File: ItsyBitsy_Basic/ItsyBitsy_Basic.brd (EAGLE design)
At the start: 47 x 20.3 mm, 3 parts

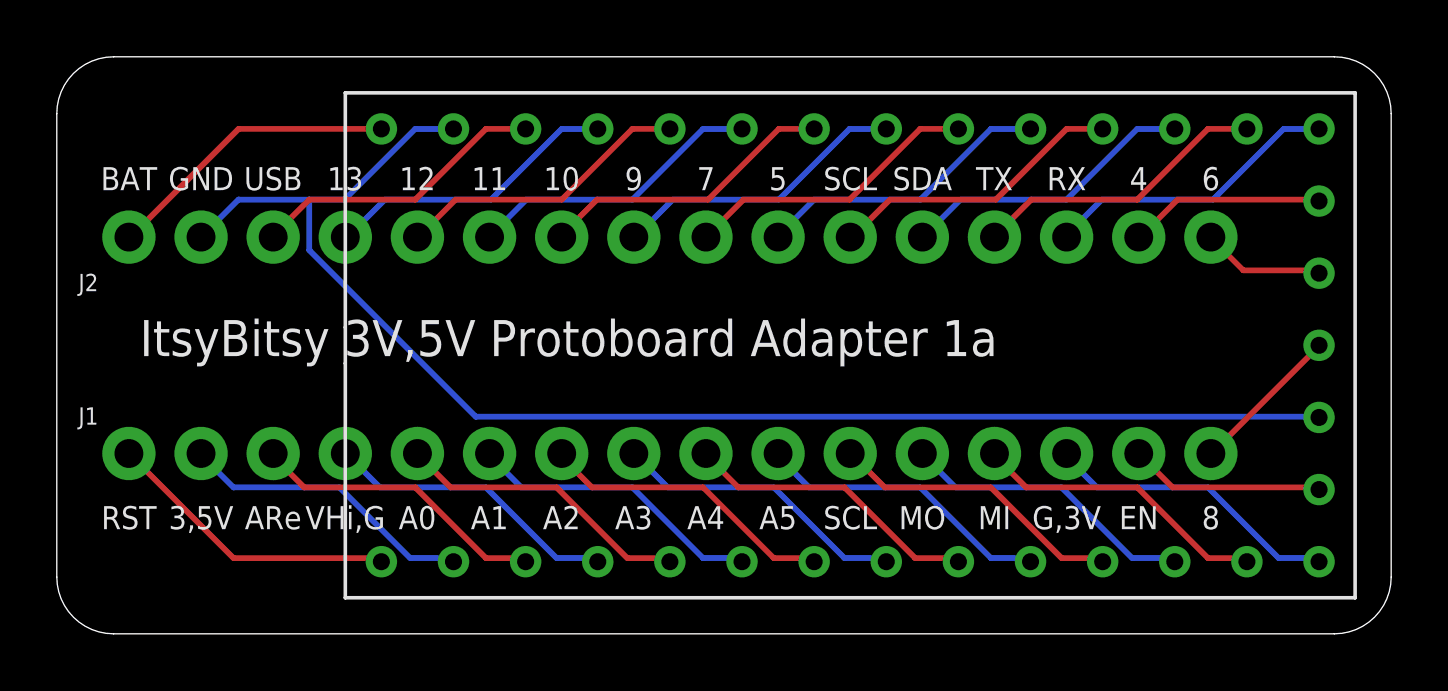
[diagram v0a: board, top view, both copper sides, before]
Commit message: enlarged ItsyBitsy holes, add CAM/Gerber zip file
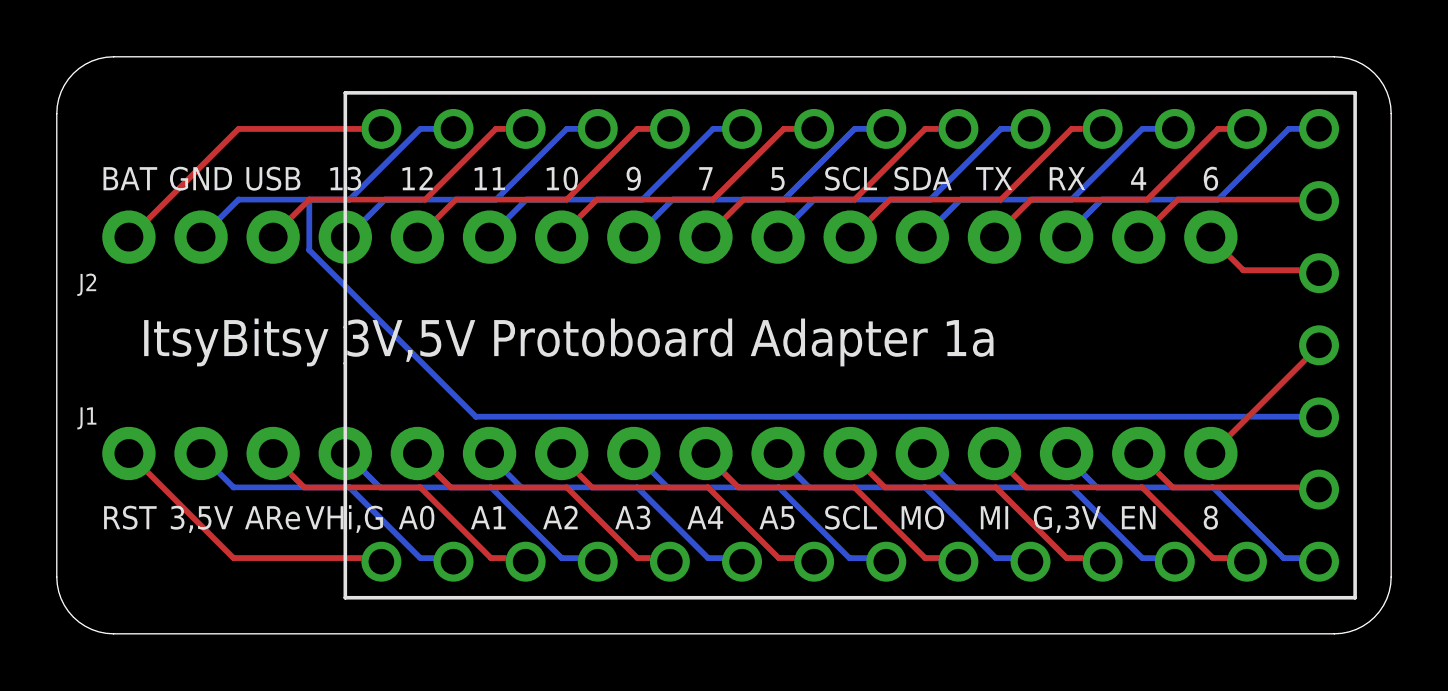
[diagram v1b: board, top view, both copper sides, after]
